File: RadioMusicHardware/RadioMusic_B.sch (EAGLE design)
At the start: 24 parts, among them U1 TEENSY_3.1_TW, U2 MCP6002, U3 TL072_

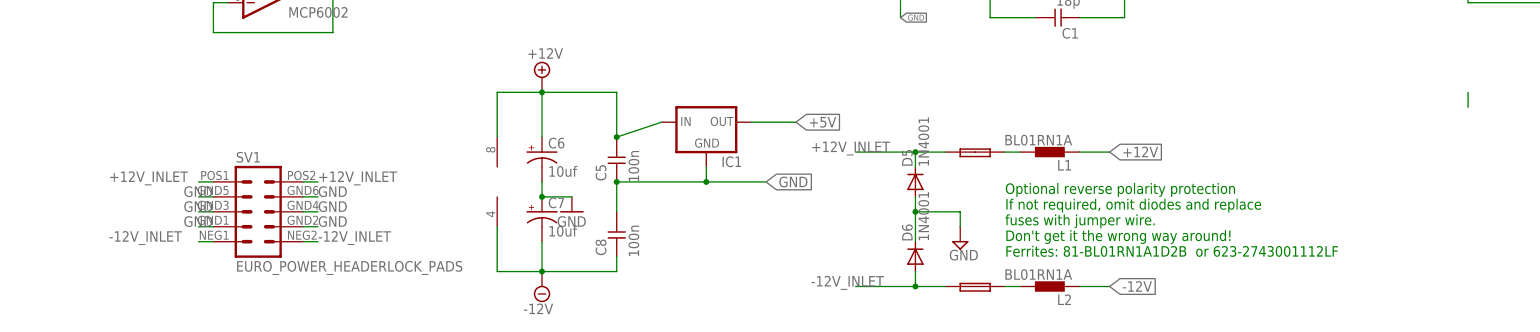
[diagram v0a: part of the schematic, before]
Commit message: starting SMD needs layout
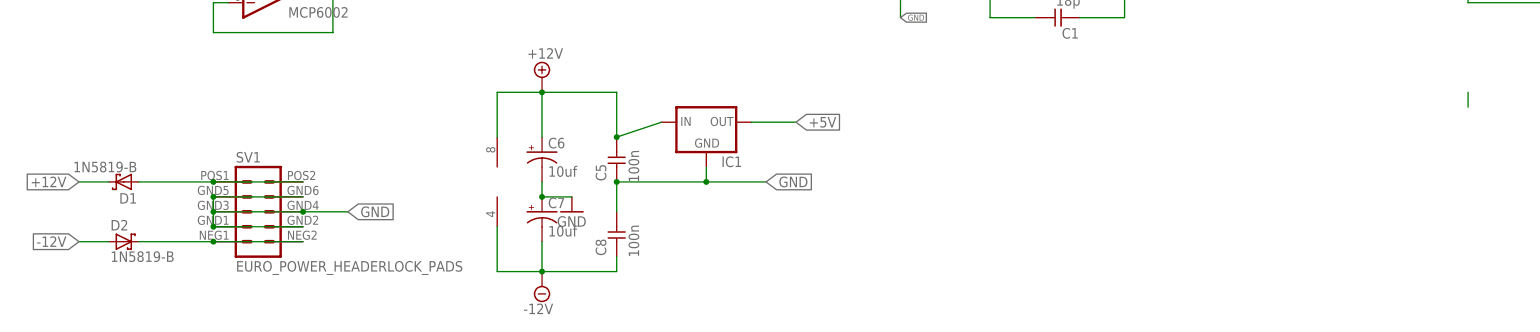
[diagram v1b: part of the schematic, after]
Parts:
- removed D5, D6: 1N4001, diode:1N4004
- removed F1, F2: FUSE, TomW:PTC_FUSEPOLY_FUSE
- removed L1, L2: BL01RN1A, inductors:BL01RN1A
- added D1, D2: 1N5819-B, diode:1N5819-B
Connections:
- removed net +12V_INLET: D5.C, F1.P$1, SV1.10, SV1.9
- removed net -12V_INLET: D6.A, F2.P$1, SV1.1, SV1.2
- removed net N$22: F1.P$2, L1.2
- removed net N$23: F2.P$2, L2.2
- new net N$2: D1.A, SV1.10, SV1.9
- new net N$6: D2.C, SV1.1, SV1.2
- net +12V: now also D1.C; no longer L1.1
- net -12V: now also D2.A; no longer L2.1
- net GND: no longer D5.A, D6.C
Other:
- note removed: "Optional reverse polarity protection If not required, omit diodes and replace fuses with jumper wire. Don't get it the wrong way around! Ferrites: 81-BL01RN1A1D2B or 623-2743001112LF"
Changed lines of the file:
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@@
 <part name="C8" library="TomW" deviceset="C-EU" device="050-024X044" value="100n"/>
 <part name="C7" library="SparkFun-Passives" deviceset="CAP_POL" device="PTH2" value="10uf"/>
-<part name="D5" library="diode" deviceset="1N4004" device="" value="1N4001"/>
-<part name="D6" library="diode" deviceset="1N4004" device="" value="1N4001"/>
-<part name="F1" library="TomW" deviceset="PTC_FUSE" device="POLY_FUSE" value="FUSE"/>
-<part name="F2" library="TomW" deviceset="PTC_FUSE" device="POLY_FUSE" value="FUSE"/>
-<part name="SUPPLY2" library="supply2" deviceset="GND" device=""/>
 <part name="U1" library="TomW" deviceset="TEENSY_3.1_TW" device=""/>
 <part name="R4" library="MusicThingModular" deviceset="RESISTOR" device="7MM" value="5.6k"/>
 <part name="C1" library="TomW" deviceset="C-EU" device="050-024X044" value="18p"/>
-<part name="L1" library="inductors" deviceset="BL0" device="1RN1A"/>
-<part name="L2" library="inductors" deviceset="BL0" device="1RN1A"/>
 <part name="JP1" library="SparkFun-Connectors" deviceset="M11" device="PTH" value="M11PTH"/>
 <part name="JP3" library="SparkFun-Connectors" deviceset="M07" device=""/>
@@
 <part name="C2" library="SparkFun-Passives" deviceset="CAP_POL" device="PTH2" value="10uf"/>
 <part name="R1" library="MusicThingModular" deviceset="RESISTOR" device="7MM" value="39k"/>
+<part name="D1" library="diode" deviceset="1N581*" device="" technology="9-B"/>
+<part name="D2" library="diode" deviceset="1N581*" device="" technology="9-B"/>
 </parts>
 <sheets>
 <sheet>
 <plain>
-<text x="142.24" y="15.24" size="1.778" layer="91">Optional reverse polarity protection
-If not required, omit diodes and replace
-fuses with jumper wire.
-Don't get it the wrong way around!
-Ferrites: 81-BL01RN1A1D2B  or 623-2743001112LF</text>
 <text x="144.78" y="91.44" size="1.27" layer="91"> SD Card Connections:
  SCLK 14
@@
 <instance part="C8" gate="G$1" x="76.2" y="20.32"/>
 <instance part="C7" gate="G$1" x="63.5" y="22.86"/>
-<instance part="D5" gate="1" x="127" y="27.94" rot="R90"/>
-<instance part="D6" gate="1" x="127" y="15.24" rot="R90"/>
-<instance part="F1" gate="G$1" x="137.16" y="33.02"/>
-<instance part="F2" gate="G$1" x="137.16" y="10.16"/>
-<instance part="SUPPLY2" gate="GND" x="134.62" y="17.78"/>
 <instance part="U1" gate="G$1" x="116.84" y="114.3"/>
 <instance part="U2" gate="A" x="17.78" y="114.3"/>
@@
 <instance part="C1" gate="G$1" x="149.86" y="55.88" rot="R90"/>
 <instance part="U2" gate="B" x="17.78" y="60.96"/>
-<instance part="L1" gate="G$1" x="149.86" y="33.02" rot="R180"/>
-<instance part="L2" gate="G$1" x="149.86" y="10.16" rot="R180"/>
 <instance part="JP1" gate="G$1" x="208.28" y="139.7" rot="MR0"/>
 <instance part="JP3" gate="G$1" x="203.2" y="106.68" rot="MR0"/>
@@
 <instance part="C2" gate="G$1" x="116.84" y="73.66" rot="R90"/>
 <instance part="R1" gate="G$1" x="124.46" y="66.04" rot="R90"/>
+<instance part="D1" gate="G$1" x="-7.62" y="27.94" rot="R180"/>
+<instance part="D2" gate="G$1" x="-7.62" y="17.78"/>
 </instances>
 <busses>
@@
 <nets>
 <net name="GND" class="2">
-<segment>
-<pinref part="SV1" gate="G$1" pin="7"/>
-<wire x1="25.4" y1="25.4" x2="22.86" y2="25.4" width="0.1524" layer="91"/>
-<label x="25.4" y="25.4" size="1.778" layer="95"/>
-</segment>
-<segment>
-<pinref part="SV1" gate="G$1" pin="5"/>
-<wire x1="25.4" y1="22.86" x2="22.86" y2="22.86" width="0.1524" layer="91"/>
-<label x="25.4" y="22.86" size="1.778" layer="95"/>
-</segment>
-<segment>
-<pinref part="SV1" gate="G$1" pin="3"/>
-<wire x1="25.4" y1="20.32" x2="22.86" y2="20.32" width="0.1524" layer="91"/>
-<label x="25.4" y="20.32" size="1.778" layer="95"/>
-</segment>
-<segment>
-<pinref part="SV1" gate="G$1" pin="8"/>
-<wire x1="5.08" y1="25.4" x2="7.62" y2="25.4" width="0.1524" layer="91"/>
-<label x="2.54" y="25.4" size="1.778" layer="95"/>
-</segment>
-<segment>
-<pinref part="SV1" gate="G$1" pin="6"/>
-<wire x1="5.08" y1="22.86" x2="7.62" y2="22.86" width="0.1524" layer="91"/>
-<label x="2.54" y="22.86" size="1.778" layer="95"/>
-</segment>
-<segment>
-<pinref part="SV1" gate="G$1" pin="4"/>
-<wire x1="5.08" y1="20.32" x2="7.62" y2="20.32" width="0.1524" layer="91"/>
-<label x="2.54" y="20.32" size="1.778" layer="95"/>
-</segment>
-<segment>
-<pinref part="D5" gate="1" pin="A"/>
-<pinref part="D6" gate="1" pin="C"/>
-<wire x1="127" y1="25.4" x2="127" y2="22.86" width="0.1524" layer="91"/>
-<pinref part="SUPPLY2" gate="GND" pin="GND"/>
-<wire x1="127" y1="22.86" x2="127" y2="17.78" width="0.1524" layer="91"/>
-<wire x1="127" y1="22.86" x2="134.62" y2="22.86" width="0.1524" layer="91"/>
-<wire x1="134.62" y1="22.86" x2="134.62" y2="20.32" width="0.1524" layer="91"/>
-<junction x="127" y="22.86"/>
-</segment>
 <segment>
 <pinref part="U1" gate="G$1" pin="AGND"/>
@@
 <wire x1="220.98" y1="71.12" x2="223.52" y2="71.12" width="0.1524" layer="91"/>
 <label x="220.98" y="71.12" size="1.016" layer="95" rot="R180" xref="yes"/>
+</segment>
+<segment>
+<pinref part="SV1" gate="G$1" pin="4"/>
+<pinref part="SV1" gate="G$1" pin="3"/>
+<wire x1="7.62" y1="20.32" x2="22.86" y2="20.32" width="0.1524" layer="91"/>
+<pinref part="SV1" gate="G$1" pin="8"/>
+<pinref part="SV1" gate="G$1" pin="7"/>
+<wire x1="7.62" y1="25.4" x2="22.86" y2="25.4" width="0.1524" layer="91"/>
+<pinref part="SV1" gate="G$1" pin="6"/>
+<pinref part="SV1" gate="G$1" pin="5"/>
+<wire x1="7.62" y1="22.86" x2="22.86" y2="22.86" width="0.1524" layer="91"/>
+<wire x1="7.62" y1="25.4" x2="7.62" y2="22.86" width="0.1524" layer="91"/>
+<junction x="7.62" y="25.4"/>
+<junction x="7.62" y="22.86"/>
+<wire x1="7.62" y1="20.32" x2="7.62" y2="22.86" width="0.1524" layer="91"/>
+<junction x="7.62" y="20.32"/>
+<wire x1="22.86" y1="22.86" x2="30.48" y2="22.86" width="0.1524" layer="91"/>
+<junction x="22.86" y="22.86"/>
+<label x="30.48" y="22.86" size="1.778" layer="95" xref="yes"/>
 </segment>
 </net>
@@
 </segment>
 <segment>
-<wire x1="160.02" y1="33.02" x2="154.94" y2="33.02" width="0.1524" layer="91"/>
-<label x="160.02" y="33.02" size="1.778" layer="95" xref="yes"/>
-<pinref part="L1" gate="G$1" pin="1"/>
+<pinref part="D1" gate="G$1" pin="C"/>
+<wire x1="-10.16" y1="27.94" x2="-15.24" y2="27.94" width="0.1524" layer="91"/>
+<label x="-15.24" y="27.94" size="1.778" layer="95" rot="R180" xref="yes"/>
 </segment>
 </net>
@@
 </segment>
 <segment>
-<label x="160.02" y="10.16" size="1.778" layer="95" xref="yes"/>
-<wire x1="160.02" y1="10.16" x2="154.94" y2="10.16" width="0.1524" layer="91"/>
-<pinref part="L2" gate="G$1" pin="1"/>
-</segment>
-</net>
-<net name="+12V_INLET" class="1">
-<segment>
-<pinref part="SV1" gate="G$1" pin="10"/>
-<wire x1="5.08" y1="27.94" x2="7.62" y2="27.94" width="0.1524" layer="91"/>
-<label x="-10.16" y="27.94" size="1.778" layer="95"/>
-</segment>
-<segment>
-<pinref part="SV1" gate="G$1" pin="9"/>
-<wire x1="25.4" y1="27.94" x2="22.86" y2="27.94" width="0.1524" layer="91"/>
-<label x="25.4" y="27.94" size="1.778" layer="95"/>
-</segment>
-<segment>
-<pinref part="F1" gate="G$1" pin="P$1"/>
-<pinref part="D5" gate="1" pin="C"/>
-<wire x1="132.08" y1="33.02" x2="127" y2="33.02" width="0.1524" layer="91"/>
-<wire x1="127" y1="33.02" x2="127" y2="30.48" width="0.1524" layer="91"/>
-<wire x1="127" y1="33.02" x2="116.84" y2="33.02" width="0.1524" layer="91"/>
-<junction x="127" y="33.02"/>
-<label x="109.22" y="33.02" size="1.778" layer="95"/>
-</segment>
-</net>
-<net name="-12V_INLET" class="1">
-<segment>
-<pinref part="SV1" gate="G$1" pin="1"/>
-<wire x1="25.4" y1="17.78" x2="22.86" y2="17.78" width="0.1524" layer="91"/>
-<label x="25.4" y="17.78" size="1.778" layer="95"/>
-</segment>
-<segment>
-<pinref part="SV1" gate="G$1" pin="2"/>
-<wire x1="5.08" y1="17.78" x2="7.62" y2="17.78" width="0.1524" layer="91"/>
-<label x="-10.16" y="17.78" size="1.778" layer="95"/>
-</segment>
-<segment>
-<pinref part="F2" gate="G$1" pin="P$1"/>
-<wire x1="116.84" y1="10.16" x2="127" y2="10.16" width="0.1524" layer="91"/>
-<label x="109.22" y="10.16" size="1.778" layer="95"/>
-<pinref part="D6" gate="1" pin="A"/>
-<wire x1="127" y1="10.16" x2="132.08" y2="10.16" width="0.1524" layer="91"/>
-<wire x1="127" y1="12.7" x2="127" y2="10.16" width="0.1524" layer="91"/>
-<junction x="127" y="10.16"/>
+<pinref part="D2" gate="G$1" pin="A"/>
+<wire x1="-10.16" y1="17.78" x2="-15.24" y2="17.78" width="0.1524" layer="91"/>
+<label x="-15.24" y="17.78" size="1.778" layer="95" rot="R180" xref="yes"/>
 </segment>
 </net>
@@
 <wire x1="195.58" y1="147.32" x2="198.12" y2="147.32" width="0.1524" layer="91"/>
 <label x="195.58" y="147.32" size="1.016" layer="95" rot="R180" xref="yes"/>
-</segment>
-</net>
-<net name="N$22" class="1">
-<segment>
-<pinref part="L1" gate="G$1" pin="2"/>
-<pinref part="F1" gate="G$1" pin="P$2"/>
-<wire x1="144.78" y1="33.02" x2="142.24" y2="33.02" width="0.1524" layer="91"/>
-</segment>
-</net>
-<net name="N$23" class="1">
-<segment>
-<pinref part="F2" gate="G$1" pin="P$2"/>
-<pinref part="L2" gate="G$1" pin="2"/>
-<wire x1="144.78" y1="10.16" x2="142.24" y2="10.16" width="0.1524" layer="91"/>
 </segment>
 </net>
@@
 </segment>
 </net>
+<net name="N$2" class="0">
+<segment>
+<pinref part="SV1" gate="G$1" pin="10"/>
+<pinref part="D1" gate="G$1" pin="A"/>
+<wire x1="7.62" y1="27.94" x2="-5.08" y2="27.94" width="0.1524" layer="91"/>
+<pinref part="SV1" gate="G$1" pin="9"/>
+<wire x1="22.86" y1="27.94" x2="7.62" y2="27.94" width="0.1524" layer="91"/>
+<junction x="7.62" y="27.94"/>
+</segment>
+</net>
+<net name="N$6" class="0">
+<segment>
+<pinref part="D2" gate="G$1" pin="C"/>
+<pinref part="SV1" gate="G$1" pin="2"/>
+<wire x1="-5.08" y1="17.78" x2="7.62" y2="17.78" width="0.1524" layer="91"/>
+<pinref part="SV1" gate="G$1" pin="1"/>
+<wire x1="22.86" y1="17.78" x2="7.62" y2="17.78" width="0.1524" layer="91"/>
+<junction x="7.62" y="17.78"/>
+</segment>
+</net>
